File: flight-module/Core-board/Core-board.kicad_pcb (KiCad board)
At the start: 4 copper layers, 141.7 x 134.1 mm, 97 parts, among them J1 Stack_Shape, J2 Conn_01x03_Pin, J3 USB_B_Micro, J4 Conn_01x06_Pin, J5 Conn_01x03_Pin, J6 Conn_01x03_Pin, J7 Conn_01x03_Pin, J8 Conn_01x03_Pin, J9 Conn_01x03_Pin, Q1 MMBT4403LT3G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

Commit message: change the USB layout
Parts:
- removed D2: D_Schottky, Diode_SMD:D_SOD-128
- added D4: D_Schottky, Diode_SMD:D_SOD-128, F.Cu at (121.8, 36.5)
- added F1: 500mA Fuse, Fuse:Fuse_0603_1608Metric, F.Cu at (118.1, 38.3)
- added J10: USB4105-GF-A, Connector_USB:USB_C_Receptacle_GCT_USB4105-xx-A_16P_TopMnt_Horizontal, F.Cu at (134.5, 31.1)
- added R2: 5.1k, Resistor_SMD:R_0805_2012Metric_Pad1.20x1.40mm_HandSolder, F.Cu at (142.8, 30.6)
- added R3: 5.1k, Resistor_SMD:R_0805_2012Metric_Pad1.20x1.40mm_HandSolder, F.Cu at (145.6, 30.7)
- J3: value USB_B_Micro -> Probe_points; footprint Connector_USB:USB_Micro-B_Amphenol_10103594-0001LF_Horizontal -> Connector_PinHeader_2.54mm:PinHeader_1x04_P2.54mm_Vertical
- moved D1 7.32 mm to (121.7, 42.5), turned to 180 degrees
- moved J3 1.76 mm to (126.4, 34.1), turned to 0 degrees
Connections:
- C10 pad 1: /ESP32-S3-WROOM-1-Breakout/EN -> GND
- C10 pad 2: GND -> /ESP32-S3-WROOM-1-Breakout/EN
- C9 pad 1: /ESP32-S3-WROOM-1-Breakout/BOOT -> GND
- C9 pad 2: GND -> /ESP32-S3-WROOM-1-Breakout/BOOT
- J3 pad 1: Net-(D2-A) -> +5V
- J3 pad 2: /ESP32-S3-WROOM-1-Breakout/USB_D- -> /ESP32-S3-WROOM-1-Breakout/USB_D+
- J3 pad 3: /ESP32-S3-WROOM-1-Breakout/USB_D+ -> /ESP32-S3-WROOM-1-Breakout/USB_D-
- J3 pad 4: unconnected-(J3-ID-Pad4) -> GND
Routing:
- net /ESP32-S3-WROOM-1-Breakout/USB_D+: track 37.9 -> 54.5 mm
- net Net-(J10-CC2): track 0.00 -> 12.6 mm
- net Net-(J10-CC1): track 0.00 -> 12.3 mm
- net /ESP32-S3-WROOM-1-Breakout/USB_D-: track 38.2 -> 48.0 mm
- net GND: track 246.3 -> 238.6 mm, vias 26 -> 28
- net Net-(D2-A): track 6.31 -> 0.00 mm
- net +3.3V: track 395.6 -> 401.9 mm, vias 5 -> 6
- net Net-(D4-A): track 0.00 -> 3.99 mm
- net +5V: track 82.5 -> 85.6 mm, vias 8 -> 7

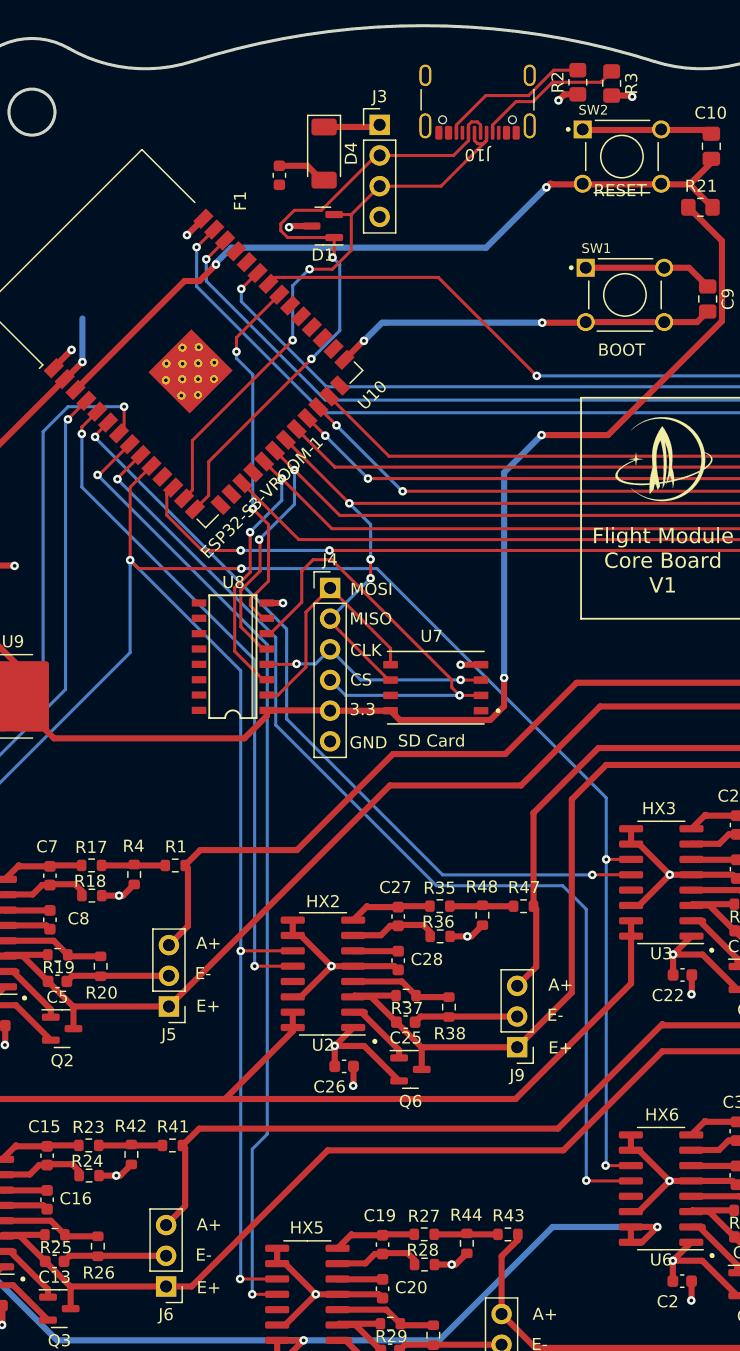
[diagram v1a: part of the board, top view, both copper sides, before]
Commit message: added silkscreen cover
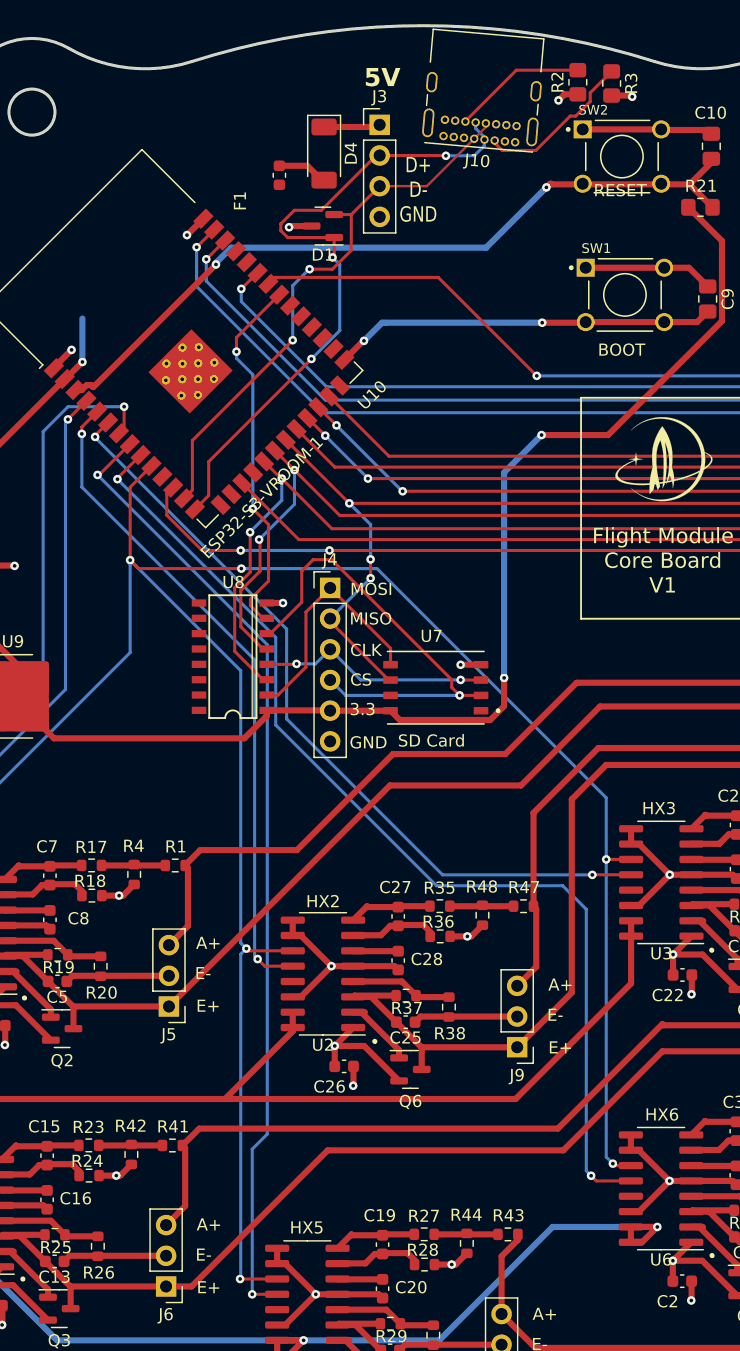
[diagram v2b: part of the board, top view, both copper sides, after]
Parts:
- J10: footprint Connector_USB:USB_C_Receptacle_GCT_USB4105-xx-A_16P_TopMnt_Horizontal -> Connector_USB:USB_C_Receptacle_GCT_USB4085
- moved J10 5.45 mm to (137.6, 35.6), turned to 175 degrees
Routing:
- net /ESP32-S3-WROOM-1-Breakout/USB_D-: track 48.0 -> 46.2 mm
- net Net-(J10-CC2): track 12.6 -> 11.1 mm
- net Net-(J10-CC1): track 12.3 -> 13.3 mm
- net /ESP32-S3-WROOM-1-Breakout/USB_D+: track 54.5 -> 55.3 mm, vias 2 -> 3
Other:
- board text added: "5V"
- board text added: "D+ D- GND"

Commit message: in the middle of updating micro usb
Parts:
- SW1, SW2: footprint 1825910-6:SW_1825910-6-4 -> Button_Switch_THT:SW_Push_2P1T_Toggle_CK_PVA1xxH1xxxxxxV2
- moved R21 12.8 mm to (140.1, 41.0)
- moved C9 11.8 mm to (141.8, 47.4)
- moved C10 11.5 mm to (142.4, 37.2)
- moved G*** 4.01 mm to (150.0, 65.8)
- moved J10 3.05 mm to (137.6, 32.5)
- moved SW2 1.48 mm to (146.8, 35.3)
- moved SW1 1.47 mm to (146.9, 46.8)
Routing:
- net +3.3V: track 401.9 -> 372.5 mm
- net GND: track 238.4 -> 219.6 mm, vias 28 -> 29
- net /ESP32-S3-WROOM-1-Breakout/USB_D-: track 46.2 -> 57.9 mm
- net /ESP32-S3-WROOM-1-Breakout/USB_D+: track 55.3 -> 61.9 mm, vias 3 -> 2
- net /ESP32-S3-WROOM-1-Breakout/BOOT: track 31.0 -> 34.0 mm
- net /ESP32-S3-WROOM-1-Breakout/EN: track 63.7 -> 66.1 mm, vias 2 -> 1
- net Net-(J10-CC1): track 13.3 -> 15.1 mm
- net Net-(J10-CC2): track 11.1 -> 9.82 mm

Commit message: ON GOD ITS DONE
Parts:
- removed D4: D_Schottky, Diode_SMD:D_SOD-128
- removed F1: 500mA Fuse, Fuse:Fuse_0603_1608Metric
- removed J10: USB4105-GF-A, Connector_USB:USB_C_Receptacle_GCT_USB4085
- removed R2, R3: 5.1k, Resistor_SMD:R_0805_2012Metric_Pad1.20x1.40mm_HandSolder
- added D2: D_Schottky, Diode_SMD:D_SOD-128, F.Cu at (137.3, 35.0)
- added J11: 10118194-0011LF, MicroUSB:AMPHENOL_10118194-0011LF, F.Cu at (133.5, 27.7)
- SW1, SW2: footprint Button_Switch_THT:SW_Push_2P1T_Toggle_CK_PVA1xxH1xxxxxxV2 -> 1825910-6:SW_1825910-6-4
- moved SW2 14.0 mm to (149.7, 49.1)
- moved SW1 8.61 mm to (149.4, 38.5)
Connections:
- SW1 pad 3: /ESP32-S3-WROOM-1-Breakout/BOOT -> /ESP32-S3-WROOM-1-Breakout/EN
- SW1 pad 4: /ESP32-S3-WROOM-1-Breakout/BOOT -> /ESP32-S3-WROOM-1-Breakout/EN
- SW2 pad 3: /ESP32-S3-WROOM-1-Breakout/EN -> /ESP32-S3-WROOM-1-Breakout/BOOT
- SW2 pad 4: /ESP32-S3-WROOM-1-Breakout/EN -> /ESP32-S3-WROOM-1-Breakout/BOOT
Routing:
- net +3.3V: track 372.5 -> 391.0 mm
- net Net-(J10-CC1): track 15.1 -> 0.00 mm
- net /ESP32-S3-WROOM-1-Breakout/USB_D-: track 57.9 -> 45.4 mm
- net /ESP32-S3-WROOM-1-Breakout/USB_D+: track 61.9 -> 50.8 mm, vias 2 -> 4
- net Net-(J10-CC2): track 9.82 -> 0.00 mm
- net +5V: track 85.6 -> 93.2 mm, vias 7 -> 8
- net GND: track 219.6 -> 226.0 mm, vias 29 -> 27
- net Net-(D4-A): track 3.99 -> 0.00 mm
- net Net-(D2-K): track 0.00 -> 3.69 mm
- net /ESP32-S3-WROOM-1-Breakout/BOOT: track 34.0 -> 34.9 mm
